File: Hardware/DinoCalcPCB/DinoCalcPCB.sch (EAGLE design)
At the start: 11 parts, among them J1 AVR_SPI, U1 ATMEGA328P_PDIP

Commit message: Ready to etch for testing
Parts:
- JP2: value (none) -> LEDS
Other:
- note removed: "James R. Bundick"
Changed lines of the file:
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@@
 <part name="U1" library="SparkFun-DigitalIC" deviceset="ATMEGA328P_PDIP" device=""/>
 <part name="JP1" library="SparkFun-Connectors" deviceset="M02" device="PTH" value="BATTERY"/>
-<part name="JP2" library="SparkFun-Connectors" deviceset="M03" device="PTH"/>
+<part name="JP2" library="SparkFun-Connectors" deviceset="M03" device="PTH" value="LEDS"/>
 <part name="JP3" library="SparkFun-Connectors" deviceset="M08" device="1X08" value="KEYPAD"/>
 <part name="LOGO1" library="SparkFun-Aesthetics" deviceset="OSHW-LOGO" device="L"/>
@@
 <plain>
 <text x="238.76" y="7.62" size="2.54" layer="91" font="vector">1v0</text>
-<text x="165.1" y="7.62" size="3.81" layer="91" font="vector">James R. Bundick</text>
 </plain>
 <instances>
@@
 <wire x1="53.34" y1="137.16" x2="55.88" y2="137.16" width="0.1524" layer="91"/>
 <pinref part="S1" gate="S" pin="2"/>
-<wire x1="55.88" y1="134.62" x2="55.88" y2="137.16" width="0.1524" layer="91"/>
-<junction x="55.88" y="137.16"/>
+<wire x1="55.88" y1="134.62" x2="53.34" y2="134.62" width="0.1524" layer="91"/>
+<junction x="53.34" y="134.62"/>
 </segment>
 <segment>

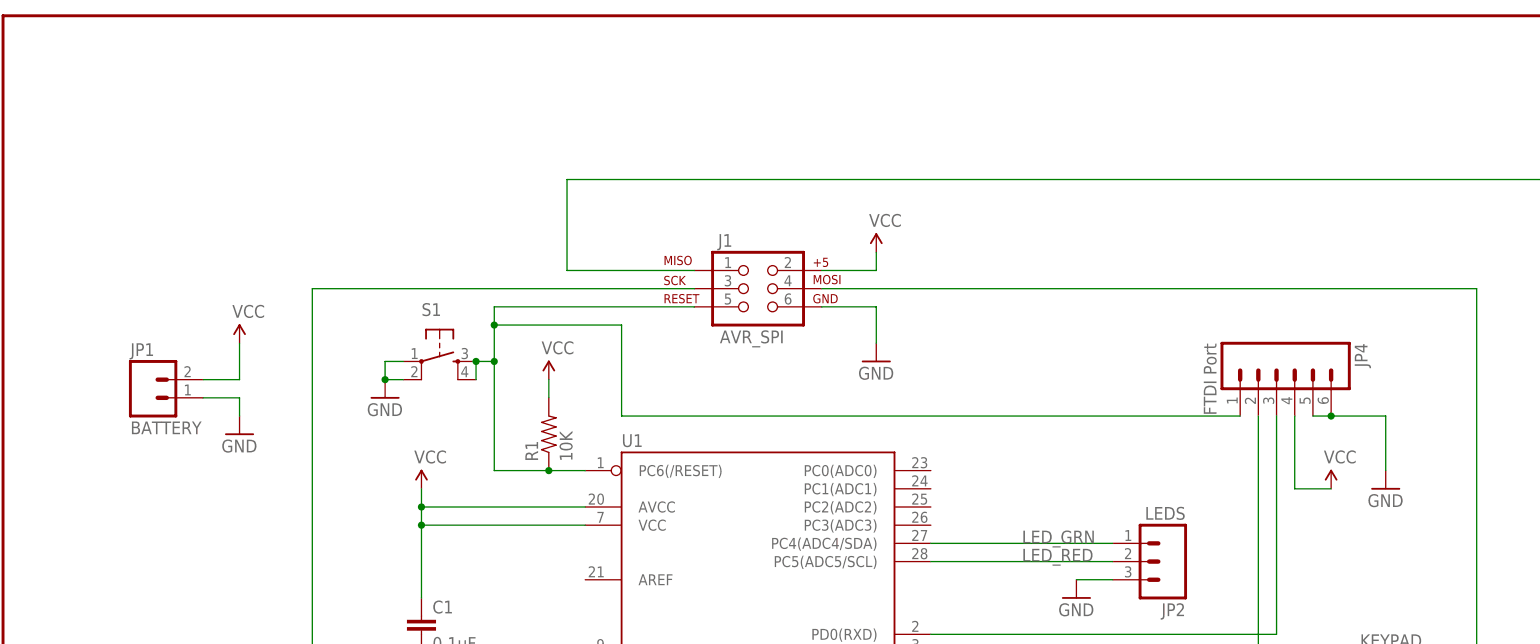
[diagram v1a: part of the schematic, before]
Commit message: Added diode
Diode added for reverse battery protection.  Also optimized placement of
components a little bit.
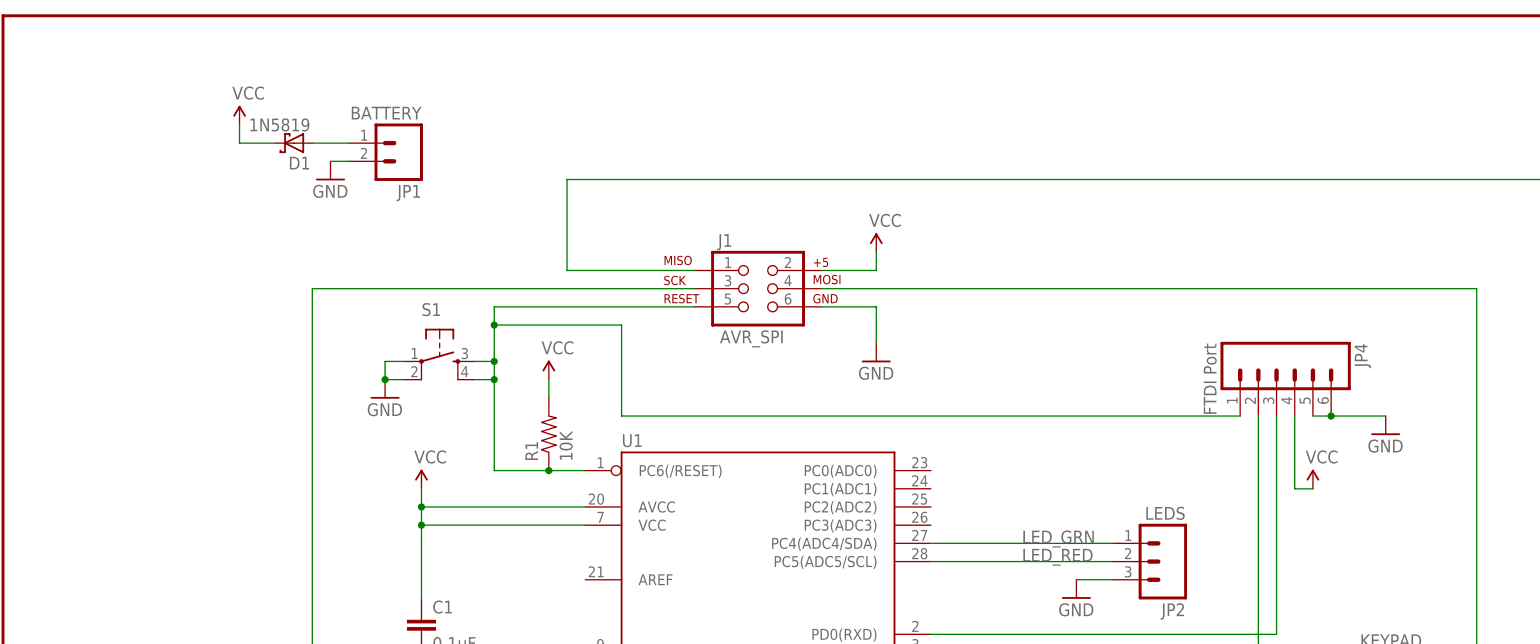
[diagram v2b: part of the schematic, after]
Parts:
- added D1: 1N5819, adafruit:SCHOTTKY-DIODECB417-15
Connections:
- new net N$11: D1.A, JP1.1
- net GND: now also JP1.2; no longer JP1.1
- net VCC: now also D1.C; no longer JP1.2
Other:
- moved on the sheet: JP1
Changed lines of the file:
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@@
 <layer number="106" name="bPlate" color="7" fill="1" visible="no" active="yes"/>
 <layer number="107" name="Crop" color="7" fill="1" visible="no" active="yes"/>
+<layer number="108" name="fp8" color="7" fill="1" visible="no" active="yes"/>
+<layer number="109" name="fp9" color="7" fill="1" visible="no" active="yes"/>
+<layer number="110" name="fp0" color="7" fill="1" visible="no" active="yes"/>
+<layer number="111" name="LPC17xx" color="7" fill="1" visible="yes" active="yes"/>
+<layer number="112" name="tSilk" color="7" fill="1" visible="yes" active="yes"/>
 <layer number="116" name="Patch_BOT" color="9" fill="4" visible="no" active="yes"/>
 <layer number="121" name="_tsilk" color="7" fill="1" visible="no" active="yes"/>
 <layer number="122" name="_bsilk" color="7" fill="1" visible="no" active="yes"/>
+<layer number="123" name="tTestmark" color="7" fill="1" visible="no" active="yes"/>
+<layer number="124" name="bTestmark" color="7" fill="1" visible="no" active="yes"/>
 <layer number="125" name="_tNames" color="7" fill="1" visible="no" active="yes"/>
+<layer number="126" name="_bNames" color="7" fill="1" visible="yes" active="yes"/>
+<layer number="127" name="_tValues" color="7" fill="1" visible="yes" active="yes"/>
+<layer number="128" name="_bValues" color="7" fill="1" visible="yes" active="yes"/>
+<layer number="131" name="tAdjust" color="7" fill="1" visible="no" active="yes"/>
+<layer number="132" name="bAdjust" color="7" fill="1" visible="no" active="yes"/>
 <layer number="144" name="Drill_legend" color="7" fill="1" visible="no" active="yes"/>
 <layer number="151" name="HeatSink" color="7" fill="1" visible="no" active="yes"/>
+<layer number="152" name="_bDocu" color="7" fill="1" visible="yes" active="yes"/>
 <layer number="199" name="Contour" color="7" fill="1" visible="yes" active="yes"/>
 <layer number="200" name="200bmp" color="1" fill="10" visible="no" active="yes"/>
@@
 <layer number="223" name="223bmp" color="24" fill="1" visible="no" active="no"/>
 <layer number="224" name="224bmp" color="25" fill="1" visible="no" active="no"/>
+<layer number="248" name="Housing" color="7" fill="1" visible="yes" active="yes"/>
+<layer number="249" name="Edge" color="7" fill="1" visible="yes" active="yes"/>
 <layer number="250" name="Descript" color="3" fill="1" visible="no" active="no"/>
 <layer number="251" name="SMDround" color="12" fill="11" visible="no" active="no"/>
@@
 <part name="JP3" library="SparkFun-Connectors" deviceset="M08" device="1X08" value="KEYPAD"/>
 <part name="LOGO1" library="SparkFun-Aesthetics" deviceset="OSHW-LOGO" device="L"/>
-<part name="FRAME1" library="SparkFun-Aesthetics" deviceset="FRAME-LETTER" device=""/>
 <part name="J1" library="SparkFun-Connectors" deviceset="AVR_SPI_PRG_6" device="OFFSET_PADS" value="AVR_SPI"/>
 <part name="GND1" library="SparkFun-Aesthetics" deviceset="GND" device=""/>
@@
 <part name="GND6" library="SparkFun-Aesthetics" deviceset="GND" device=""/>
 <part name="SUPPLY5" library="SparkFun-Aesthetics" deviceset="VCC" device=""/>
+<part name="FRAME1" library="SparkFun-Aesthetics" deviceset="FRAME-LETTER" device=""/>
+<part name="D1" library="adafruit" deviceset="SCHOTTKY-DIODE" device="CB417-15" value="1N5819"/>
 </parts>
 <sheets>
@@
 <instances>
 <instance part="U1" gate="G$1" x="104.14" y="96.52"/>
-<instance part="JP1" gate="G$1" x="20.32" y="132.08"/>
+<instance part="JP1" gate="G$1" x="55.88" y="167.64" rot="R180"/>
 <instance part="JP2" gate="G$1" x="162.56" y="109.22" rot="R180"/>
 <instance part="JP3" gate="G$1" x="193.04" y="86.36" rot="R180"/>
 <instance part="LOGO1" gate="G$1" x="233.68" y="48.26"/>
-<instance part="FRAME1" gate="G$1" x="0" y="0"/>
-<instance part="FRAME1" gate="G$2" x="147.32" y="0"/>
 <instance part="J1" gate="G$1" x="104.14" y="147.32"/>
 <instance part="GND1" gate="1" x="149.86" y="104.14"/>
@@
 <instance part="GND3" gate="1" x="121.92" y="137.16"/>
 <instance part="SUPPLY1" gate="1" x="58.42" y="119.38"/>
-<instance part="SUPPLY2" gate="1" x="33.02" y="139.7"/>
-<instance part="GND4" gate="1" x="33.02" y="127"/>
+<instance part="SUPPLY2" gate="1" x="33.02" y="170.18"/>
+<instance part="GND4" gate="1" x="45.72" y="162.56"/>
 <instance part="C1" gate="G$1" x="58.42" y="99.06"/>
 <instance part="SUPPLY3" gate="1" x="121.92" y="152.4"/>
@@
 <instance part="GND5" gate="1" x="53.34" y="132.08"/>
 <instance part="JP4" gate="G$1" x="177.8" y="134.62" rot="R270"/>
-<instance part="GND6" gate="1" x="193.04" y="119.38"/>
-<instance part="SUPPLY5" gate="1" x="185.42" y="119.38"/>
+<instance part="GND6" gate="1" x="193.04" y="127"/>
+<instance part="SUPPLY5" gate="1" x="182.88" y="119.38"/>
+<instance part="FRAME1" gate="G$1" x="0" y="0"/>
+<instance part="FRAME1" gate="G$2" x="147.32" y="0"/>
+<instance part="D1" gate="G$1" x="40.64" y="167.64" rot="R180"/>
 </instances>
 <busses>
@@
 </segment>
 <segment>
-<pinref part="JP1" gate="G$1" pin="1"/>
-<wire x1="27.94" y1="132.08" x2="33.02" y2="132.08" width="0.1524" layer="91"/>
-<wire x1="33.02" y1="132.08" x2="33.02" y2="129.54" width="0.1524" layer="91"/>
 <pinref part="GND4" gate="1" pin="GND"/>
+<pinref part="JP1" gate="G$1" pin="2"/>
+<wire x1="48.26" y1="165.1" x2="45.72" y2="165.1" width="0.1524" layer="91"/>
 </segment>
 <segment>
@@
 <wire x1="185.42" y1="129.54" x2="193.04" y2="129.54" width="0.1524" layer="91"/>
 <pinref part="GND6" gate="1" pin="GND"/>
-<wire x1="193.04" y1="129.54" x2="193.04" y2="121.92" width="0.1524" layer="91"/>
 <pinref part="JP4" gate="G$1" pin="5"/>
 <wire x1="182.88" y1="129.54" x2="185.42" y2="129.54" width="0.1524" layer="91"/>
@@
 <junction x="76.2" y="121.92"/>
 <wire x1="76.2" y1="121.92" x2="68.58" y2="121.92" width="0.1524" layer="91"/>
-<wire x1="68.58" y1="121.92" x2="68.58" y2="137.16" width="0.1524" layer="91"/>
+<wire x1="68.58" y1="121.92" x2="68.58" y2="134.62" width="0.1524" layer="91"/>
 <pinref part="S1" gate="S" pin="3"/>
+<wire x1="68.58" y1="134.62" x2="68.58" y2="137.16" width="0.1524" layer="91"/>
 <wire x1="68.58" y1="137.16" x2="68.58" y2="142.24" width="0.1524" layer="91"/>
 <wire x1="68.58" y1="142.24" x2="68.58" y2="144.78" width="0.1524" layer="91"/>
@@
 <junction x="68.58" y="142.24"/>
 <pinref part="S1" gate="S" pin="4"/>
-<wire x1="66.04" y1="134.62" x2="66.04" y2="137.16" width="0.1524" layer="91"/>
-<junction x="66.04" y="137.16"/>
+<wire x1="66.04" y1="134.62" x2="68.58" y2="134.62" width="0.1524" layer="91"/>
+<junction x="68.58" y="134.62"/>
 </segment>
 </net>
@@
 </segment>
 <segment>
-<pinref part="JP1" gate="G$1" pin="2"/>
-<wire x1="27.94" y1="134.62" x2="33.02" y2="134.62" width="0.1524" layer="91"/>
-<pinref part="SUPPLY2" gate="1" pin="VCC"/>
-<wire x1="33.02" y1="134.62" x2="33.02" y2="139.7" width="0.1524" layer="91"/>
-</segment>
-<segment>
 <pinref part="J1" gate="G$1" pin="2"/>
 <pinref part="SUPPLY3" gate="1" pin="VCC"/>
@@
 <pinref part="SUPPLY5" gate="1" pin="VCC"/>
 <wire x1="180.34" y1="129.54" x2="180.34" y2="119.38" width="0.1524" layer="91"/>
-<wire x1="180.34" y1="119.38" x2="185.42" y2="119.38" width="0.1524" layer="91"/>
+<wire x1="180.34" y1="119.38" x2="182.88" y2="119.38" width="0.1524" layer="91"/>
+</segment>
+<segment>
+<pinref part="D1" gate="G$1" pin="C"/>
+<wire x1="38.1" y1="167.64" x2="33.02" y2="167.64" width="0.1524" layer="91"/>
+<pinref part="SUPPLY2" gate="1" pin="VCC"/>
+<wire x1="33.02" y1="167.64" x2="33.02" y2="170.18" width="0.1524" layer="91"/>
 </segment>
 </net>
@@
 </segment>
 </net>
+<net name="N$11" class="0">
+<segment>
+<pinref part="JP1" gate="G$1" pin="1"/>
+<pinref part="D1" gate="G$1" pin="A"/>
+<wire x1="48.26" y1="167.64" x2="43.18" y2="167.64" width="0.1524" layer="91"/>
+</segment>
+</net>

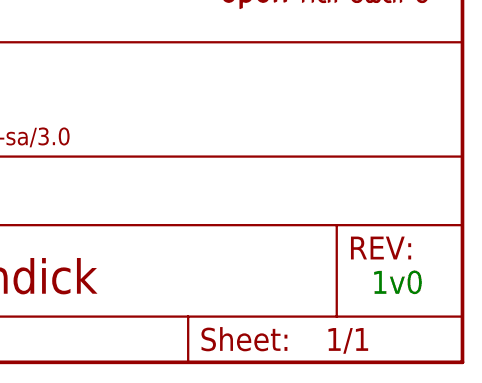
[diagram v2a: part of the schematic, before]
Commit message: Updated Version Numbering
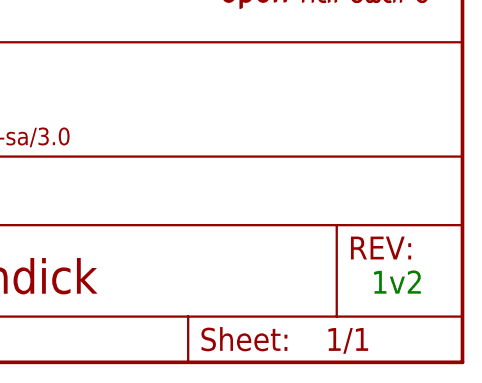
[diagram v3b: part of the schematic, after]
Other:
- note added: "1v2"
- note removed: "1v0"
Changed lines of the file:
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@@
 <sheet>
 <plain>
-<text x="238.76" y="7.62" size="2.54" layer="91" font="vector">1v0</text>
+<text x="238.76" y="7.62" size="2.54" layer="91" font="vector">1v2</text>
 </plain>
 <instances>
